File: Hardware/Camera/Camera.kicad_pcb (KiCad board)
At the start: 4 copper layers, 46.7 x 75.9 mm, 65 parts, among them J1 Power, J2 ICC Out, J3 USB_B_Mini, J4 SWDIO, J5 Header Pins, J6 Camer Interface, Q1 AO3401A, SW1 SW_SPDT, U1 STM32F407ZGT6, U2 LM317L_SOT-89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

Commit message: Small improvements for pre-routing
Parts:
- moved C10 13.9 mm to (138.2, 115.1), turned to 180 degrees
- moved R13 9.76 mm to (141.7, 115.8), turned to 90 degrees
- moved C13 4.20 mm to (121.4, 94.2), turned to 180 degrees
- moved C2 3.18 mm to (149.1, 81.5)
- moved C18 3.07 mm to (135.1, 112.5)
- moved C19 2.54 mm to (146.1, 69.1)
- moved R19 2.54 mm to (148.3, 69.3)
- moved U3 2.54 mm to (146.1, 72.9)
- moved C12 2.54 mm to (140.8, 73.0)
- moved C14 2.54 mm to (141.0, 69.6)
- moved L2 2.54 mm to (137.8, 73.0)
- moved R18 2.54 mm to (150.1, 71.1)
- moved U2 2.29 mm to (132.6, 71.6)
- moved C4 1.98 mm to (147.8, 79.5), turned to 0 degrees
- moved C3 1.93 mm to (128.3, 102.1), turned to 180 degrees
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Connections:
- net CAM_DOVDD renamed +3V3
- net CAM_GND renamed GND
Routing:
- added copper zone on In2.Cu, net +3.3VA
- added copper zone on In1.Cu, net GND

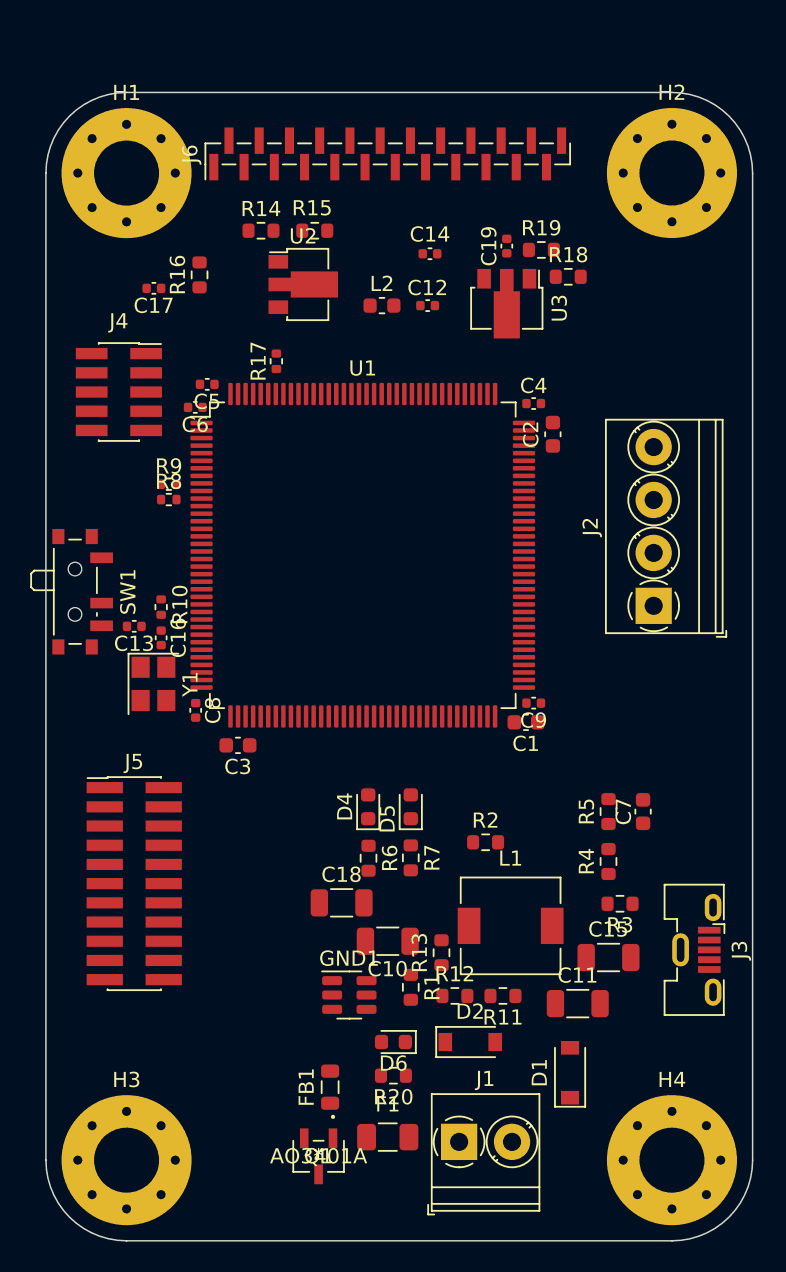
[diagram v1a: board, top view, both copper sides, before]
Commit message: Optimizing camera placement
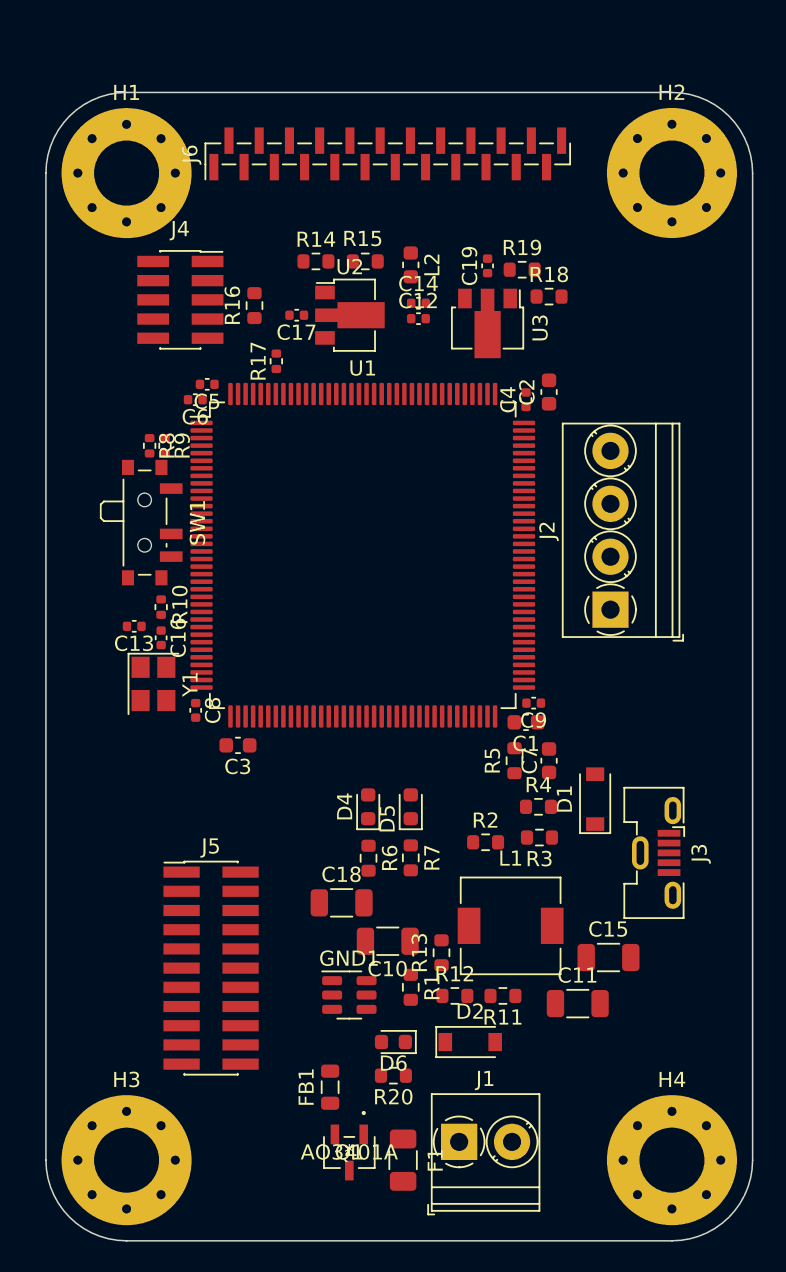
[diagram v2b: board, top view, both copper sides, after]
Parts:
- moved D1 18.2 mm to (151.9, 105.7)
- moved C17 9.61 mm to (132.2, 73.7)
- moved J5 7.55 mm to (126.5, 116.8)
- moved J4 7.33 mm to (124.5, 72.6)
- moved C7 7.07 mm to (148.8, 103.1)
- moved R5 7.07 mm to (146.6, 103.1)
- moved J3 6.94 mm to (156.0, 109.2)
- moved R3 6.90 mm to (148.2, 108.2)
- moved SW1 6.49 mm to (122.4, 87.4)
- moved R4 5.88 mm to (148.1, 106.2), turned to 0 degrees
- moved R16 4.16 mm to (129.4, 73.0)
- moved R14 4.16 mm to (133.4, 70.1)
- moved R15 3.91 mm to (136.7, 70.1)
- moved R8 3.78 mm to (122.4, 82.3), turned to -90 degrees
- moved U2 3.70 mm to (135.7, 73.7)
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
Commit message: Finished initial placement
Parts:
- moved J3 35.6 mm to (120.4, 107.2), turned to 90 degrees
- moved J5 31.6 mm to (154.9, 103.1), turned to 180 degrees
- moved D1 30.9 mm to (122.4, 114.8)
- moved R3 25.7 mm to (126.5, 121.9), turned to 0 degrees
- moved R5 22.8 mm to (131.1, 119.9), turned to 180 degrees
- moved R4 19.3 mm to (134.6, 119.9), turned to 180 degrees
- moved R11 15.4 mm to (130.6, 116.3)
- moved R13 15.3 mm to (126.5, 116.8)
- moved R12 14.7 mm to (128.0, 116.8), turned to -90 degrees
- moved R2 10.6 mm to (135.6, 114.0), turned to 180 degrees
- moved R20 10.1 mm to (130.6, 117.9)
- moved FB1 9.24 mm to (126.5, 119.9), turned to 0 degrees
- moved GND1 7.94 mm to (129.5, 113.5)
- moved D6 7.16 mm to (133.1, 117.1), turned to 90 degrees
- moved C18 5.86 mm to (129.5, 110.7)
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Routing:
- removed copper zone on In2.Cu, net +3.3VA
- removed copper zone on In1.Cu, net GND
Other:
- board size 46.7 x 75.9 mm -> 42.7 x 78.2 mm

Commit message: Basic routing done
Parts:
- J5: value Header Pins -> Breakout; footprint Connector_PinHeader_1.27mm:PinHeader_2x11_P1.27mm_Vertical_SMD -> Connector_PinHeader_1.27mm:PinHeader_1x20_P1.27mm_Vertical
- moved J4 31.5 mm to (156.0, 71.1), turned to 180 degrees
- moved C7 27.2 mm to (136.7, 76.7), turned to 180 degrees
- moved J5 11.8 mm to (157.5, 91.6), turned to 0 degrees
- moved FB1 11.7 mm to (138.2, 118.9), turned to 90 degrees
- moved R18 5.91 mm to (145.5, 67.6)
- moved R19 5.57 mm to (142.4, 67.6)
- moved C19 5.50 mm to (141.4, 66.0)
- moved J2 5.08 mm to (154.4, 88.1)
- moved R8 4.82 mm to (124.0, 86.9), turned to 90 degrees
- moved C11 2.87 mm to (152.9, 113.3), turned to 90 degrees
- moved U3 2.77 mm to (143.8, 71.6)
- moved R9 2.59 mm to (124.0, 84.8)
- moved F1 2.54 mm to (136.7, 127.0)
- moved Q1 2.54 mm to (133.6, 126.5)
- moved C3 2.03 mm to (128.8, 103.1)
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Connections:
- J5 pad 1: +3V3 -> RCC_MCO_1
- J5 pad 10: GPIO0 -> unconnected-(J5-Pad10)
- J5 pad 11: GPIO1 -> unconnected-(J5-Pad11)
- J5 pad 13: GPIO3 -> GPIO1
- J5 pad 14: GPIO4 -> GPIO0
- J5 pad 15: GPIO5 -> USART2_TX
- J5 pad 16: GPIO6 -> USART2_RX
- J5 pad 17: GPIO7 -> I2C2_SDA
- J5 pad 18: USART3_TX -> I2C2_SCL
- J5 pad 19: RCC_MCO_1 -> GND
- J5 pad 2: GND -> GPIO7
- J5 pad 20: USART3_RX -> +3V3
- J5 pad 3: USART2_TX -> GPIO6
- J5 pad 4: SPI2_SCK -> GPIO5
- J5 pad 5: USART2_RX -> GPIO4
- J5 pad 6: SPI2_MISO -> GPIO3
- J5 pad 7: I2C2_SCL -> USART3_RX
- J5 pad 8: SPI2_MOSI -> USART3_TX
- J5 pad 9: I2C2_SDA -> unconnected-(J5-Pad9)
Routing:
- net GND: track 0.00 -> 30.3 mm
- net DCMI0: track 0.00 -> 29.6 mm
- net DCMI1: track 0.00 -> 29.4 mm
- net +3V3: track 0.00 -> 29.3 mm
- net Net-(D1-Pad1): track 0.00 -> 23.2 mm
- net BUCK_SW: track 0.00 -> 18.8 mm
- net RCC_MCO_1: track 0.00 -> 17.8 mm, vias 0 -> 2
- net BUCK_IN: track 0.00 -> 14.4 mm
- net USART6_RX: track 0.00 -> 12.4 mm
- net USART3_TX: track 0.00 -> 12.0 mm
- net USART3_RX: track 0.00 -> 11.7 mm
- net GPIO3: track 0.00 -> 11.4 mm
- net HSE_IN: track 0.00 -> 11.2 mm
- net GPIO4: track 0.00 -> 11.1 mm
- net GPIO5: track 0.00 -> 10.7 mm
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- added copper zone on In2.Cu, net +3V3
- added copper zone on In1.Cu, net GND

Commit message: About to re-do layout
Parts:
- added MK1: MIC, Sensor_Audio:Infineon_PG-LLGA-5-1, F.Cu at (128.9, 76.6)
- moved C19 10.3 mm to (145.4, 75.6), turned to 0 degrees
- moved C12 9.33 mm to (131.4, 77.1), turned to -90 degrees
- moved C14 8.82 mm to (132.5, 77.1), turned to -90 degrees
- moved L2 8.47 mm to (134.5, 76.6), turned to 180 degrees
- moved U3 7.37 mm to (145.2, 78.9)
- moved C17 7.20 mm to (126.0, 77.3)
- moved R19 6.46 mm to (144.9, 73.5), turned to 90 degrees
- moved R18 6.09 mm to (146.7, 73.5), turned to -90 degrees
- moved C2 5.14 mm to (148.1, 83.8)
- moved C1 4.97 mm to (146.9, 105.5)
- moved C13 4.97 mm to (120.5, 99.9)
- moved C16 4.97 mm to (122.8, 99.9)
- moved C3 4.97 mm to (128.4, 108.1)
- moved C7 4.97 mm to (136.3, 81.7)
- moved C8 4.97 mm to (126.1, 105.5)
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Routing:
- net DCMI0: track 29.6 -> 0.00 mm
- net DCMI1: track 29.4 -> 0.00 mm
- net Net-(D1-Pad1): track 23.2 -> 0.00 mm
- net RCC_MCO_1: track 17.8 -> 0.00 mm, vias 2 -> 0
- net BUCK_SW: track 18.8 -> 2.10 mm
- net USART6_RX: track 12.4 -> 0.00 mm
- net USART3_TX: track 12.0 -> 0.00 mm
- net USART3_RX: track 11.7 -> 0.00 mm
- net GPIO3: track 11.4 -> 0.00 mm
- net GPIO4: track 11.1 -> 0.00 mm
- net GPIO5: track 10.7 -> 0.00 mm
- net GPIO7: track 10.5 -> 0.00 mm
- net GPIO6: track 10.4 -> 0.00 mm
- net USART6_TX: track 9.62 -> 0.00 mm
- net +3.3VA: track 9.20 -> 0.00 mm
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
